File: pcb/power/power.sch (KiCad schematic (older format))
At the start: 49 parts, among them CON1 BARREL_JACK, P1 CONN_01X04, P2 CONN_01X04, P3 CONN_01X04, P4 USB_B, P5 CONN_01X08, P6 CONN_01X03, P7 CONN_01X03, U1 TS30013, U2 LM324QT, U3 LM2840

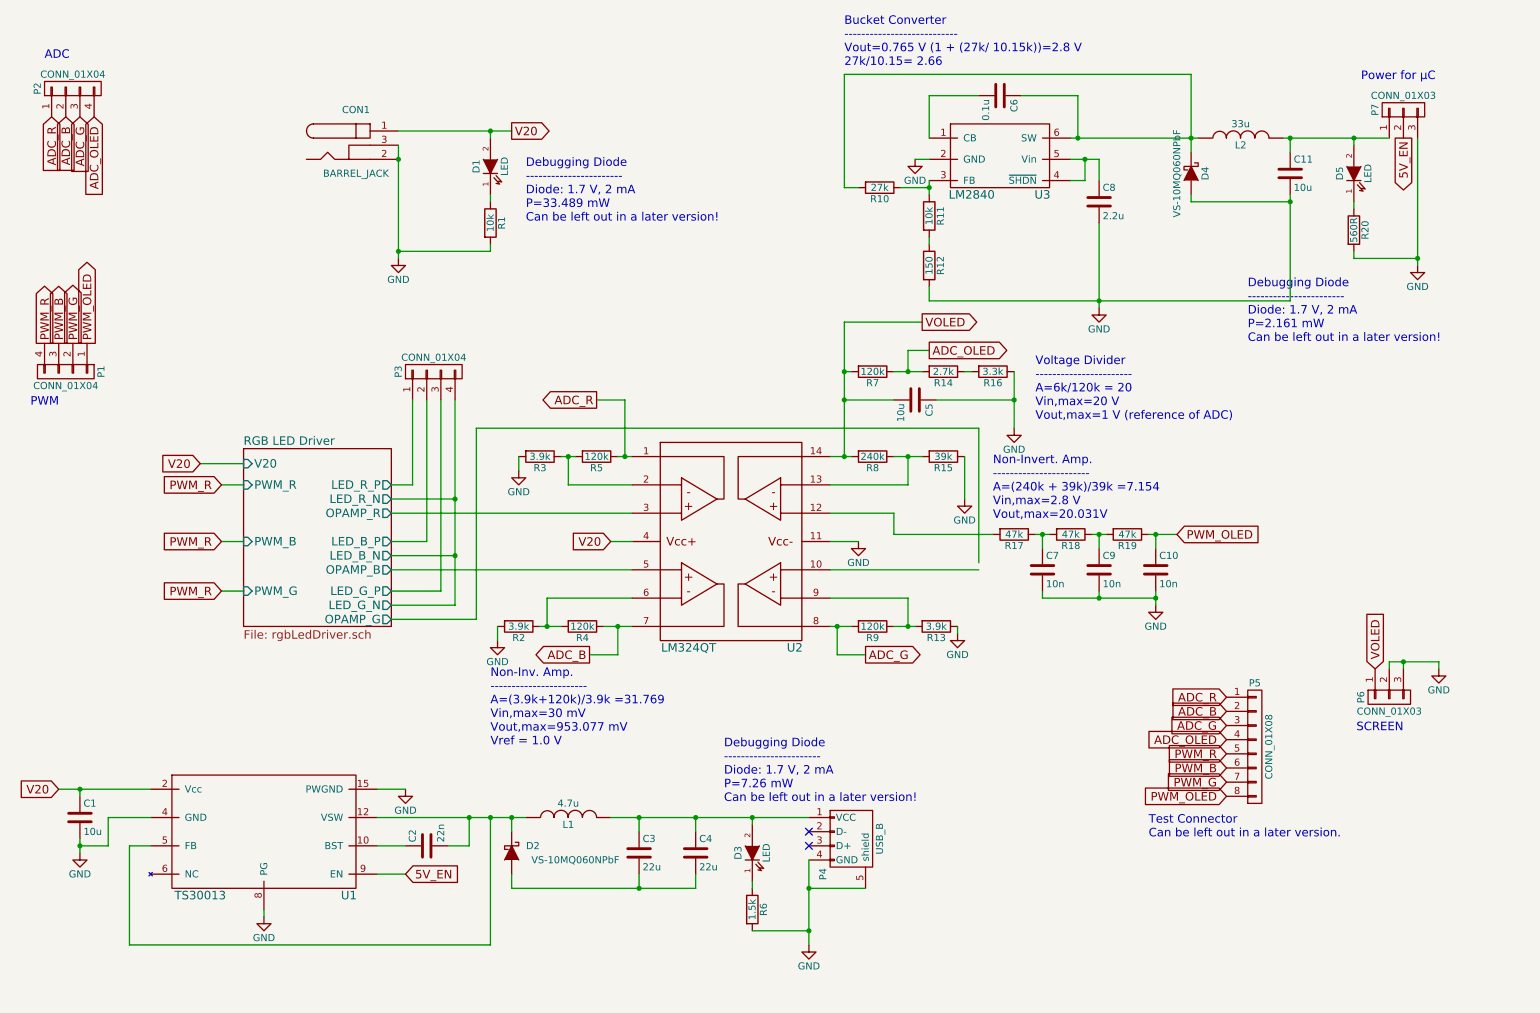
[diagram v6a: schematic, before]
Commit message: Checked all comp. of the LED Driver once more and assigned footprints.
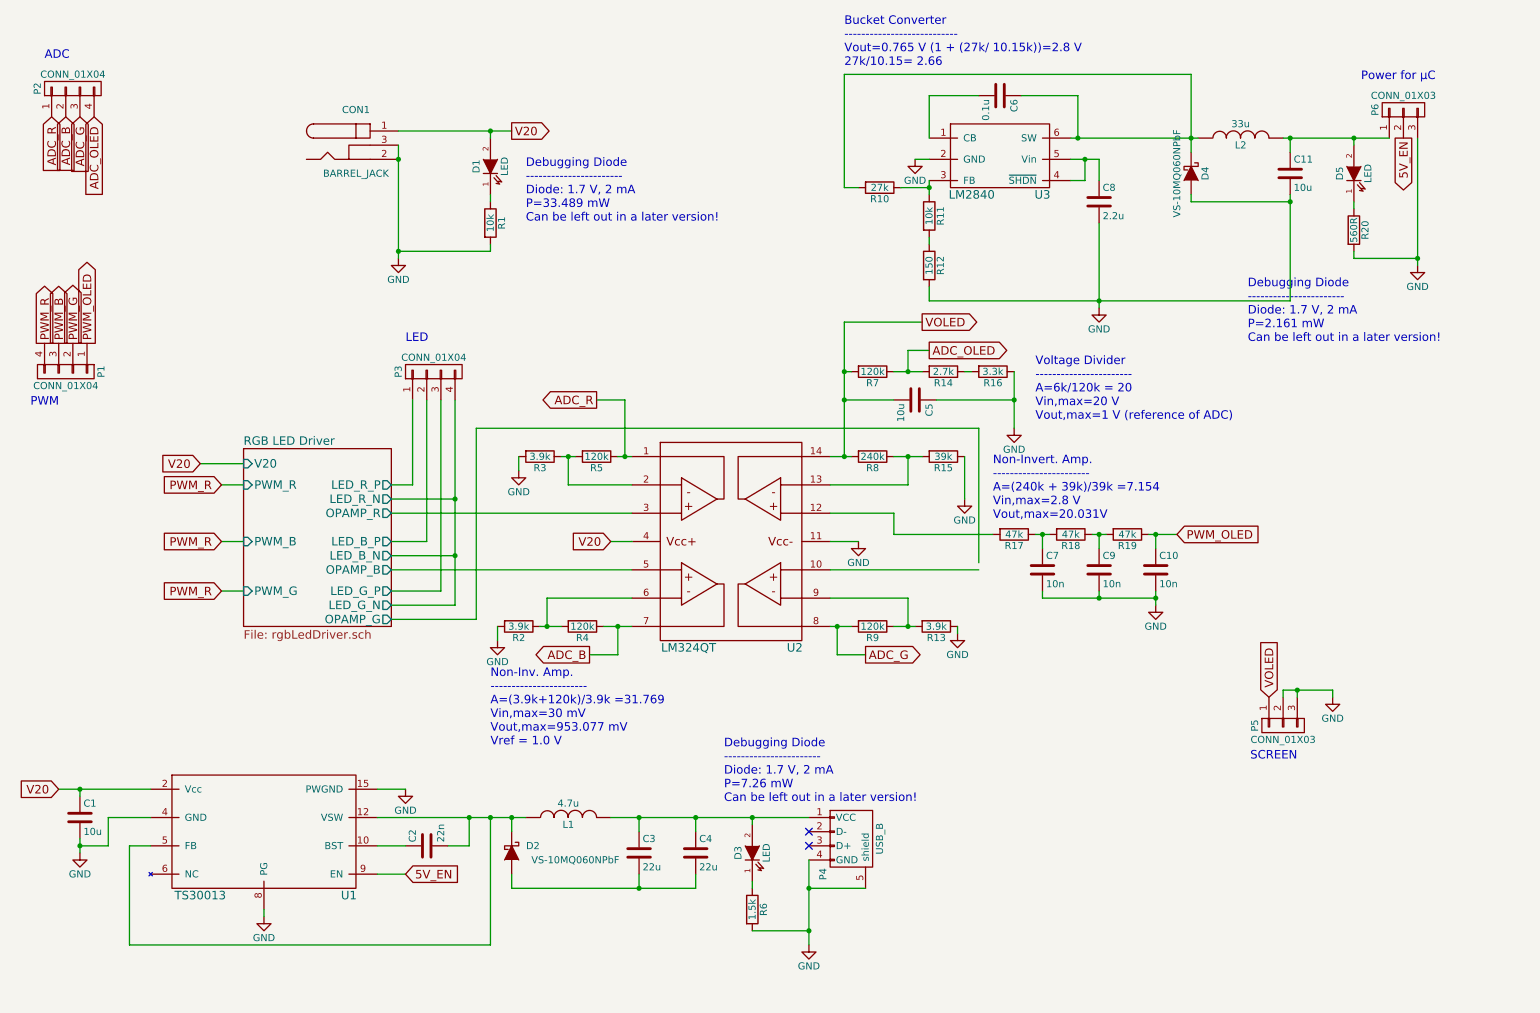
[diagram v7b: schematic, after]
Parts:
- removed P5: CONN_01X08, symbol CONN_01X08
- renumbered P6 to P5, P7 to P6
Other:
- note added: "LED"
- note removed: "Test Connector\nCan be left out in a later version."
- moved on the sheet: P5
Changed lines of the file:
@@
 $EndComp
 $Comp
-L GND #PWR01
+L GND #PWR6
 U 1 1 5838E9B2
 P 4250 3750
-F 0 "#PWR01" H 4250 3500 50  0001 C CNN
+F 0 "#PWR6" H 4250 3500 50  0001 C CNN
 F 1 "GND" H 4250 3600 50  0000 C CNN
 F 2 "" H 4250 3750 50  0000 C CNN
@@
 $EndComp
 $Comp
-L GND #PWR02
+L GND #PWR5
 U 1 1 5838F3B3
 P 4100 4950
-F 0 "#PWR02" H 4100 4700 50  0001 C CNN
+F 0 "#PWR5" H 4100 4700 50  0001 C CNN
 F 1 "GND" H 4100 4800 50  0000 C CNN
 F 2 "" H 4100 4950 50  0000 C CNN
@@
 $EndComp
 $Comp
-L GND #PWR03
+L GND #PWR10
 U 1 1 58391691
 P 7350 4900
-F 0 "#PWR03" H 7350 4650 50  0001 C CNN
+F 0 "#PWR10" H 7350 4650 50  0001 C CNN
 F 1 "GND" H 7350 4750 50  0000 C CNN
 F 2 "" H 7350 4900 50  0000 C CNN
@@
 $EndComp
 $Comp
-L GND #PWR04
+L GND #PWR11
 U 1 1 58394C0A
 P 7400 3950
-F 0 "#PWR04" H 7400 3700 50  0001 C CNN
+F 0 "#PWR11" H 7400 3700 50  0001 C CNN
 F 1 "GND" H 7400 3800 50  0000 C CNN
 F 2 "" H 7400 3950 50  0000 C CNN
@@
 $EndComp
 $Comp
-L GND #PWR05
+L GND #PWR14
 U 1 1 58395B51
 P 8750 4700
-F 0 "#PWR05" H 8750 4450 50  0001 C CNN
+F 0 "#PWR14" H 8750 4450 50  0001 C CNN
 F 1 "GND" H 8750 4550 50  0000 C CNN
 F 2 "" H 8750 4700 50  0000 C CNN
@@
 V20
 $Comp
-L GND #PWR06
+L GND #PWR8
 U 1 1 5839C2CB
 P 6650 4250
-F 0 "#PWR06" H 6650 4000 50  0001 C CNN
+F 0 "#PWR8" H 6650 4000 50  0001 C CNN
 F 1 "GND" H 6650 4100 50  0000 C CNN
 F 2 "" H 6650 4250 50  0000 C CNN
@@
 Text Notes 800  3300 0    60   ~ 0
 PWM
-Text Notes 10500 5600 2    60   ~ 0
+Text Notes 9750 5800 2    60   ~ 0
 SCREEN
 Text Notes 10200 1000 0    60   ~ 0
 Power for µC\n
 $Comp
-L GND #PWR07
+L GND #PWR3
 U 1 1 583C8E04
 P 3400 2250
-F 0 "#PWR07" H 3400 2000 50  0001 C CNN
+F 0 "#PWR3" H 3400 2000 50  0001 C CNN
 F 1 "GND" H 3400 2100 50  0000 C CNN
 F 2 "" H 3400 2250 50  0000 C CNN
@@
 $EndComp
 $Comp
-L GND #PWR08
+L GND #PWR12
 U 1 1 583CC537
 P 7750 3450
-F 0 "#PWR08" H 7750 3200 50  0001 C CNN
+F 0 "#PWR12" H 7750 3200 50  0001 C CNN
 F 1 "GND" H 7750 3300 50  0000 C CNN
 F 2 "" H 7750 3450 50  0000 C CNN
@@
 ADC_R
 $Comp
-L GND #PWR09
+L GND #PWR15
 U 1 1 583EB242
-P 10750 5150
-F 0 "#PWR09" H 10750 4900 50  0001 C CNN
-F 1 "GND" H 10750 5000 50  0000 C CNN
-F 2 "" H 10750 5150 50  0000 C CNN
-F 3 "" H 10750 5150 50  0000 C CNN
-	1    10750 5150
+P 10000 5350
+F 0 "#PWR15" H 10000 5100 50  0001 C CNN
+F 1 "GND" H 10000 5200 50  0000 C CNN
+F 2 "" H 10000 5350 50  0000 C CNN
+F 3 "" H 10000 5350 50  0000 C CNN
+	1    10000 5350
 	-1   0    0    -1
 $EndComp
 $Comp
-L GND #PWR010
+L GND #PWR16
 U 1 1 583EC5FB
 P 10600 2300
-F 0 "#PWR010" H 10600 2050 50  0001 C CNN
+F 0 "#PWR16" H 10600 2050 50  0001 C CNN
 F 1 "GND" H 10600 2150 50  0000 C CNN
 F 2 "" H 10600 2300 50  0000 C CNN
@@
 Text GLabel 1250 1250 3    60   Input ~ 0
 ADC_OLED
-Text GLabel 10300 5150 1    60   Input ~ 0
+Text GLabel 9550 5350 1    60   Input ~ 0
 VOLED
 $Comp
@@
 $EndComp
 $Comp
-L GND #PWR011
+L GND #PWR4
 U 1 1 58404311
 P 3450 6000
-F 0 "#PWR011" H 3450 5750 50  0001 C CNN
+F 0 "#PWR4" H 3450 5750 50  0001 C CNN
 F 1 "GND" H 3450 5850 50  0000 C CNN
 F 2 "" H 3450 6000 50  0000 C CNN
@@
 $EndComp
 $Comp
-L GND #PWR012
+L GND #PWR1
 U 1 1 58404317
 P 1150 6450
-F 0 "#PWR012" H 1150 6200 50  0001 C CNN
+F 0 "#PWR1" H 1150 6200 50  0001 C CNN
 F 1 "GND" H 1150 6300 50  0000 C CNN
 F 2 "" H 1150 6450 50  0000 C CNN
@@
 $EndComp
 $Comp
-L GND #PWR013
+L GND #PWR2
 U 1 1 5840432D
 P 2450 6900
-F 0 "#PWR013" H 2450 6650 50  0001 C CNN
+F 0 "#PWR2" H 2450 6650 50  0001 C CNN
 F 1 "GND" H 2450 6750 50  0000 C CNN
 F 2 "" H 2450 6900 50  0000 C CNN
@@
 $EndComp
 $Comp
-L GND #PWR014
+L GND #PWR9
 U 1 1 584064F9
 P 7050 1550
-F 0 "#PWR014" H 7050 1300 50  0001 C CNN
+F 0 "#PWR9" H 7050 1300 50  0001 C CNN
 F 1 "GND" H 7050 1400 50  0000 C CNN
 F 2 "" H 7050 1550 50  0000 C CNN
@@
 $EndComp
 $Comp
-L GND #PWR015
+L GND #PWR13
 U 1 1 5840650B
 P 8350 2600
-F 0 "#PWR015" H 8350 2350 50  0001 C CNN
+F 0 "#PWR13" H 8350 2350 50  0001 C CNN
 F 1 "GND" H 8350 2450 50  0000 C CNN
 F 2 "" H 8350 2600 50  0000 C CNN
@@
 $EndComp
 $Comp
-L GND #PWR016
+L GND #PWR7
 U 1 1 58413E62
 P 6300 7100
-F 0 "#PWR016" H 6300 6850 50  0001 C CNN
+F 0 "#PWR7" H 6300 6850 50  0001 C CNN
 F 1 "GND" H 6300 6950 50  0000 C CNN
 F 2 "" H 6300 7100 50  0000 C CNN
@@
 Debugging Diode\n-----------------------\nDiode: 1.7 V, 2 mA\nP=33.489 mW\nCan be left out in a later version!
 $Comp
-L CONN_01X08 P5
-U 1 1 583D8F25
-P 9450 5700
-F 0 "P5" H 9450 6150 50  0000 C CNN
-F 1 "CONN_01X08" V 9550 5700 50  0000 C CNN
-F 2 "" H 9450 5700 50  0000 C CNN
-F 3 "" H 9450 5700 50  0000 C CNN
-	1    9450 5700
-	1    0    0    -1
-$EndComp
-Text GLabel 9250 5550 0    60   Input ~ 0
-ADC_G
-Text GLabel 9250 5450 0    60   Input ~ 0
-ADC_B
-Text GLabel 9250 5350 0    60   Input ~ 0
-ADC_R
-Text GLabel 9250 5650 0    60   Input ~ 0
-ADC_OLED
-Text GLabel 9250 6050 0    60   Input ~ 0
-PWM_OLED
-Text GLabel 9250 5950 0    60   Input ~ 0
-PWM_G
-Text GLabel 9250 5850 0    60   Input ~ 0
-PWM_B
-Text GLabel 9250 5750 0    60   Input ~ 0
-PWM_R
-Text Notes 8700 6350 0    60   ~ 0
-Test Connector\nCan be left out in a later version.
-$Comp
-L CONN_01X03 P7
+L CONN_01X03 P6
 U 1 1 583EB36B
 P 10500 1200
-F 0 "P7" H 10500 1400 50  0000 C CNN
+F 0 "P6" H 10500 1400 50  0000 C CNN
 F 1 "CONN_01X03" V 10600 1200 50  0000 C CNN
 F 2 "" H 10500 1200 50  0000 C CNN
@@
 $EndComp
 $Comp
-L CONN_01X03 P6
+L CONN_01X03 P5
 U 1 1 583EC068
-P 10400 5350
-F 0 "P6" H 10400 5550 50  0000 C CNN
-F 1 "CONN_01X03" V 10500 5350 50  0000 C CNN
-F 2 "" H 10400 5350 50  0000 C CNN
-F 3 "" H 10400 5350 50  0000 C CNN
-	1    10400 5350
+P 9650 5550
+F 0 "P5" H 9650 5750 50  0000 C CNN
+F 1 "CONN_01X03" V 9750 5550 50  0000 C CNN
+F 2 "" H 9650 5550 50  0000 C CNN
+F 3 "" H 9650 5550 50  0000 C CNN
+	1    9650 5550
 	0    -1   1    0
 $EndComp
@@
 Connection ~ 3400 2200
 Wire Wire Line
-	10750 5100 10750 5150
-Wire Wire Line
-	10400 5100 10750 5100
-Wire Wire Line
-	10400 5100 10400 5150
-Wire Wire Line
-	10500 5150 10500 5100
-Connection ~ 10500 5100
+	10000 5300 10000 5350
+Wire Wire Line
+	9650 5300 10000 5300
+Wire Wire Line
+	9650 5300 9650 5350
+Wire Wire Line
+	9750 5350 9750 5300
+Connection ~ 9750 5300
 Wire Wire Line
 	6900 3250 6550 3250
@@
 Text Notes 7900 3400 0    60   ~ 0
 Voltage Divider\n-----------------------\nA=6k/120k = 20\nVin,max=20 V\nVout,max=1 V (reference of ADC)
+Text Notes 3450 2850 0    60   ~ 0
+LED
 $EndSCHEMATC

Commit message: Worked on the Barrel Jack mainly, bought also a matching power supply. Nice!
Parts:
- CON1: footprint (none) -> Additional:PJ-047BH_BARREL_JACK
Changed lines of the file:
@@
 F 0 "CON1" H 3100 1700 50  0000 C CNN
 F 1 "BARREL_JACK" H 3100 1250 50  0000 C CNN
-F 2 "" H 3100 1450 50  0000 C CNN
+F 2 "Additional:PJ-047BH_BARREL_JACK" H 3100 1450 50  0001 C CNN
 F 3 "http://www.cui.com/product/resource/digikeypdf/pj-047bh.pdf" H 3100 1450 50  0001 C CNN
 F 4 "CP-047BH-ND" H 3100 1450 60  0001 C CNN "Digikey"
